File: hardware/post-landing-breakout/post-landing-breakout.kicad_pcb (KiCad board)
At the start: 2 copper layers, 94.4 x 69.4 mm, 42 parts, among them J1 DE9_Socket, J2 XT90, J3 DE9_Socket, J4 RSBL85, J6 Smol_Brain_Board, Q1 MMBT3906, SW1 SW_Slide_DPDT, U1 LM2596S-5

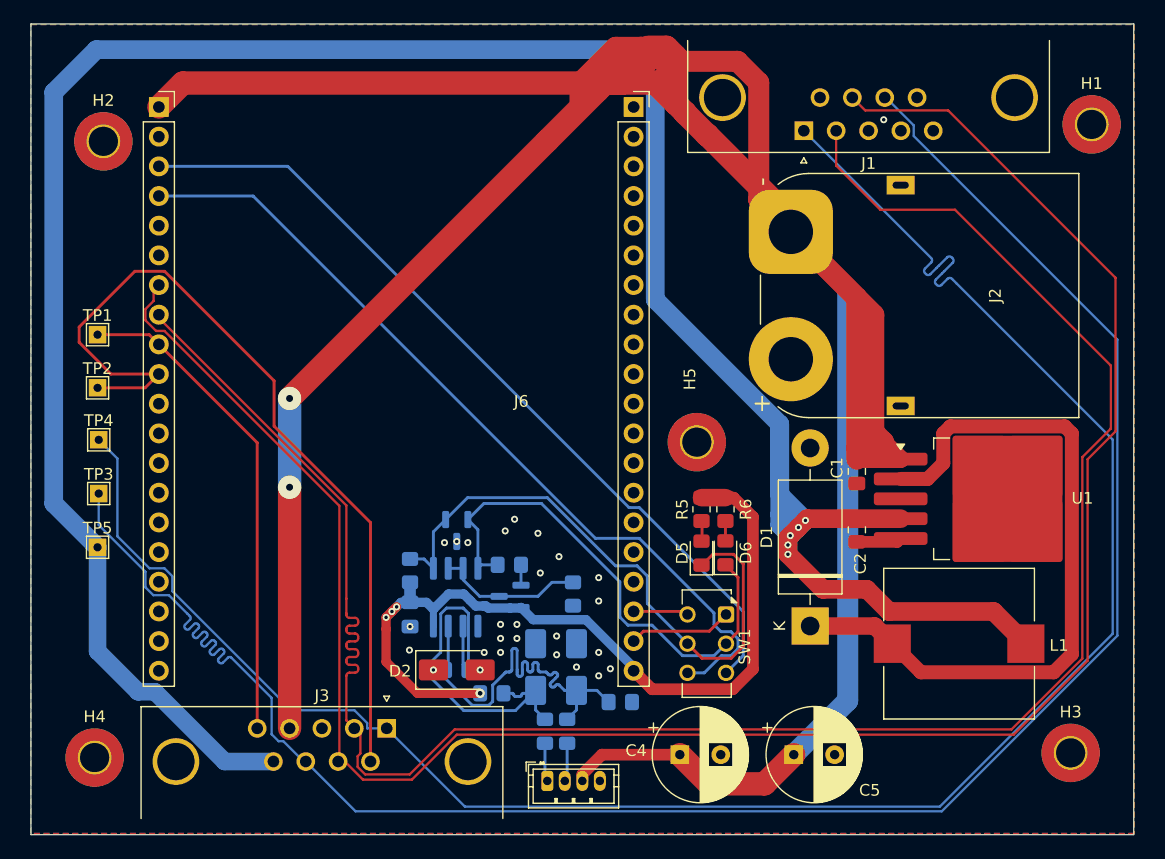
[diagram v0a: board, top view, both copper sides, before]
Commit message: feat: Changed mounting holes to 3mm, rounded corners
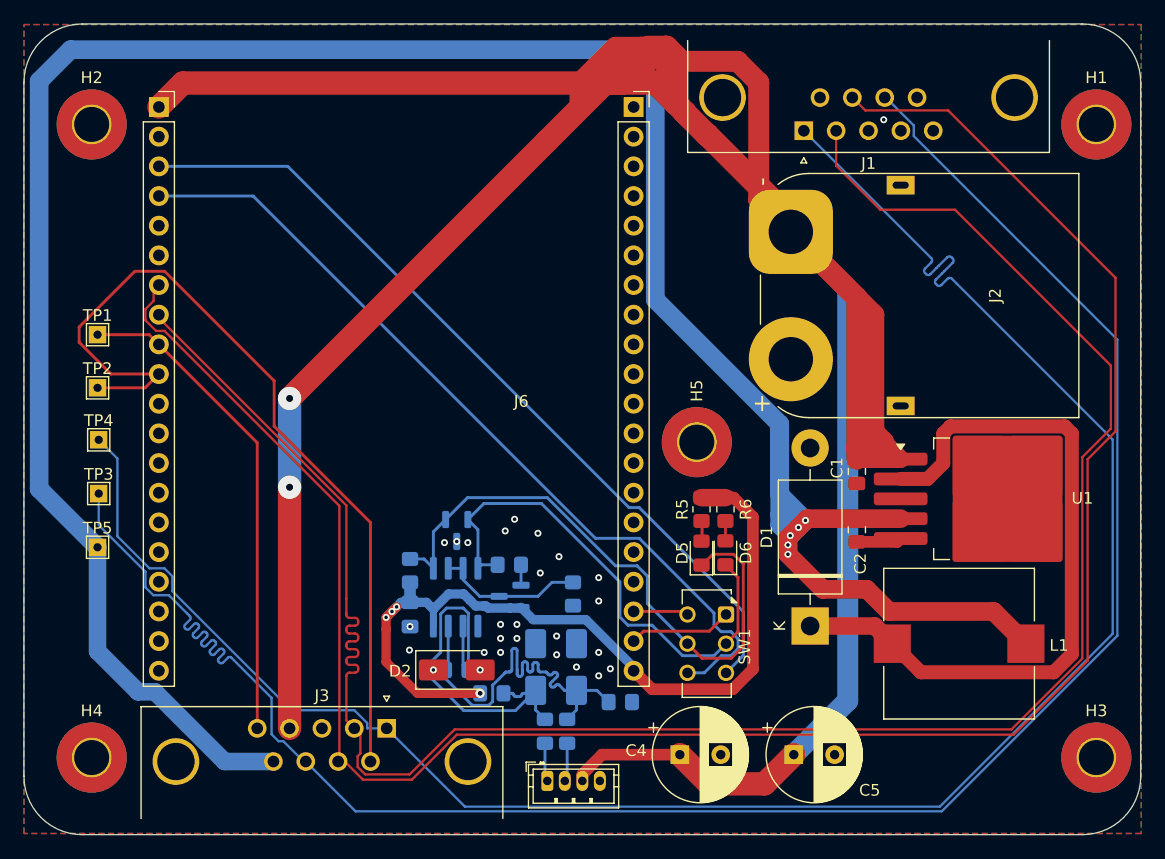
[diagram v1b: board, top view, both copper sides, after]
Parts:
- H1, H2, H3, H4, H5: footprint MountingHole:MountingHole_2.5mm_Pad_TopBottom -> MountingHole:MountingHole_3mm_Pad_TopBottom
- moved H3 2.24 mm to (165.0, 104.0)
- moved H2 1.76 mm to (79.0, 49.8)
- moved H1 0.40 mm to (165.0, 49.8)
- moved H4 0.25 mm to (79.0, 104.0)
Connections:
- J1 pad 0: GND -> (no net)
- J2 pad MP: GND -> (no net)
- J3 pad 0: GND -> (no net)
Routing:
- net +5V: track 215.9 -> 218.2 mm
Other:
- board size 94.4 x 69.4 mm -> 95.6 x 69.4 mm

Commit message: fix: Changed mounting holes to 3.2mm
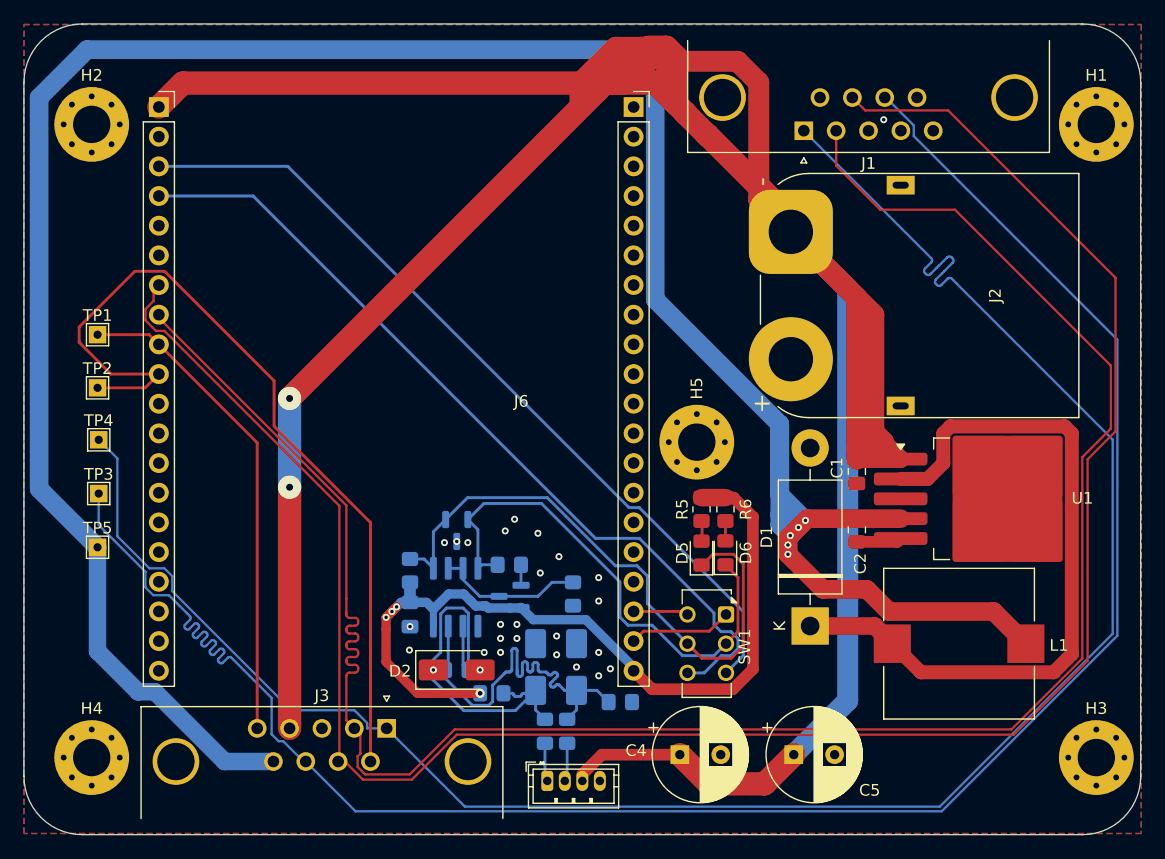
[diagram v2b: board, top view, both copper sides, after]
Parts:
- H1, H2, H3, H4, H5: footprint MountingHole:MountingHole_3mm_Pad_TopBottom -> MountingHole:MountingHole_3.2mm_M3_Pad_Via
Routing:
- net +5V: track 218.2 -> 217.4 mm
